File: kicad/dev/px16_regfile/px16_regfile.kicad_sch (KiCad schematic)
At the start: 336 parts, among them J1 Conn_02x12_Odd_Even, J2 Conn_02x12_Odd_Even, J3 Conn_02x12_Odd_Even, J4 Screw_Terminal_01x02, J5 Conn_02x12_Odd_Even, J6 Conn_02x12_Odd_Even, U1 74LS273, U10 74LS273, U11 74LS244, U12 74LS244, U13 74LS273, U14 74LS244, U15 74LS244, U16 74LS273, U17 74LS244, U18 74LS244, U19 74LS273, U2 74LS244, U20 74LS244, U21 74LS244, U22 74LS273, U23 74LS244, U24 74LS244, U25 74LS273, U26 74LS244, U27 74LS244, U28 74LS273, U29 74LS244, U3 74LS244, U30 74LS244, U31 74LS139, U32 74LS04, U33 74LS139, U34 74LS139, U35 74LS02, U36 74LS02, U37 74LS273, U38 74LS244, U39 74LS244, U4 74LS273, U40 74LS244, U41 74LS244, U42 74LS244, U43 74LS244, U44 74LS161, U45 74LS161, U46 74LS244, U47 74LS244, U48 74LS161, U49 74LS161, U5 74LS244, U50 74LS244, U51 74LS244, U52 74LS00, U53 74LS273, U54 74LS273, U55 74LS273, U56 74LS273, U57 74LS244, U58 74LS244, U59 74LS244, U6 74LS244, U60 74LS244, U7 74LS273, U8 74LS244, U9 74LS244

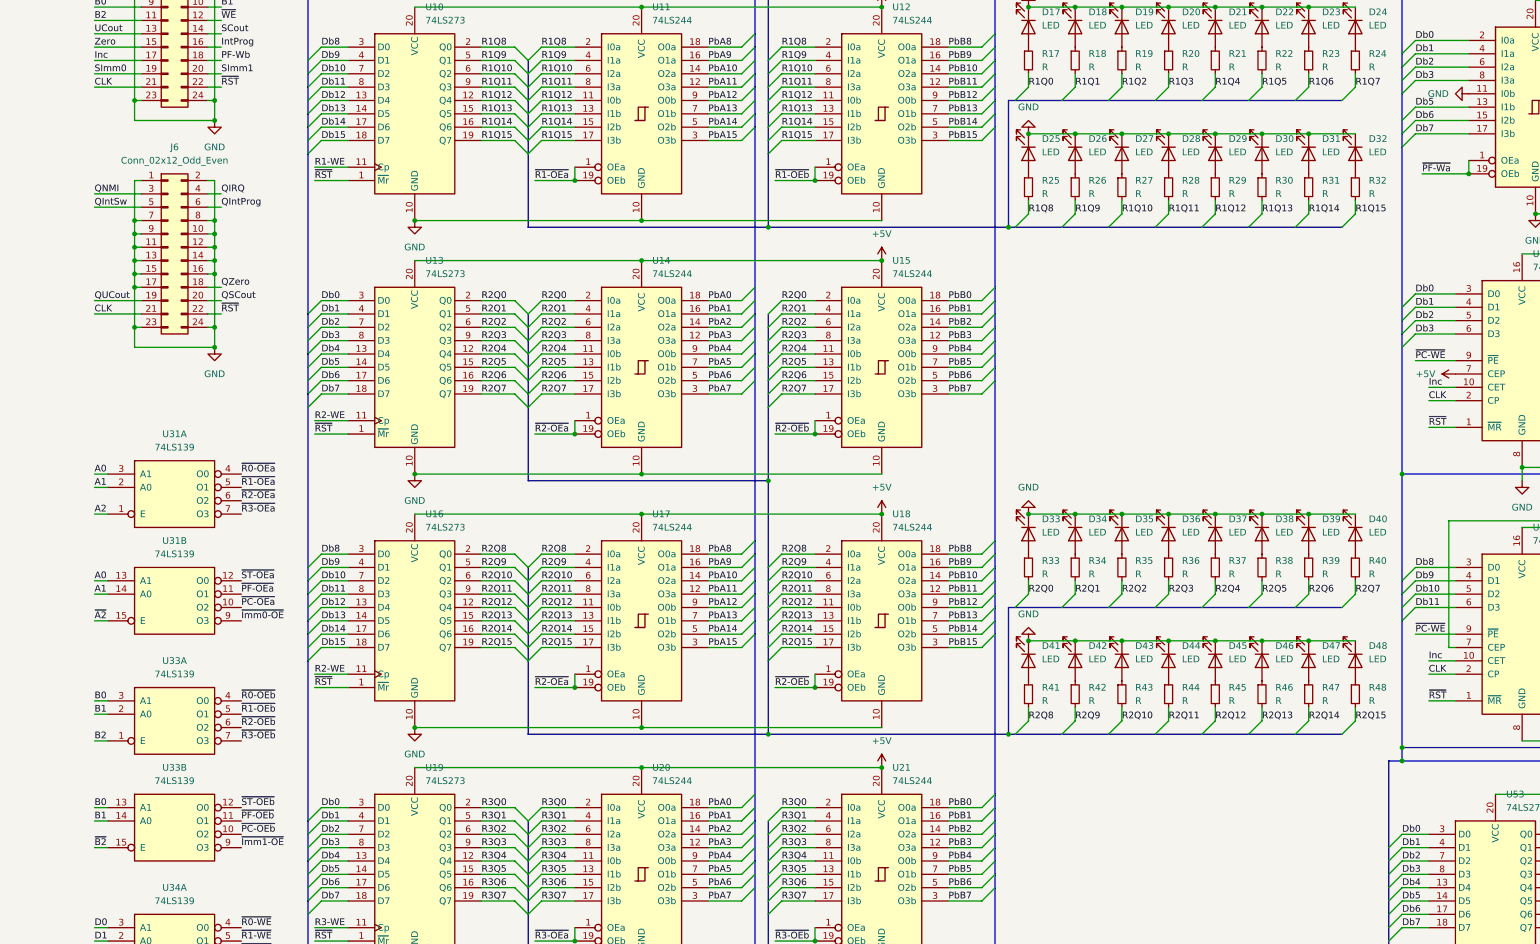
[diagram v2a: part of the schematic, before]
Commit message: Nearly completed the regfile.
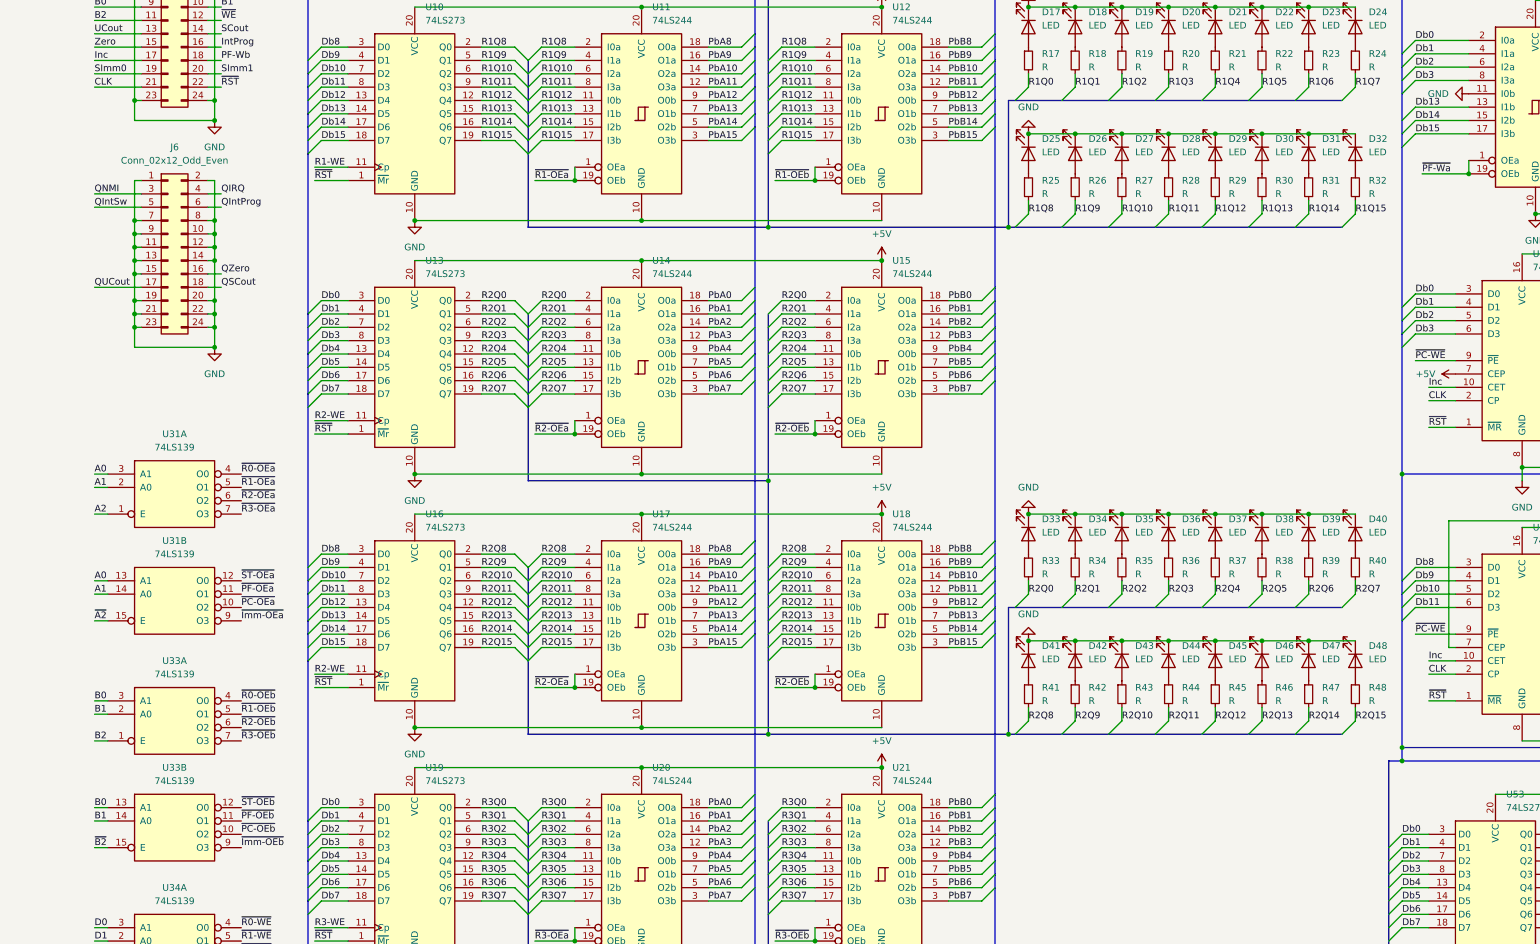
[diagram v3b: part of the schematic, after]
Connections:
- net ~{Imm0-OE} is gone; now on net ~{Imm-OEa}: U31.9 (O3)
- net ~{Imm1-OE} is gone; now on net ~{Imm-OEb}: U33.9 (O3)
- net CLK: no longer J6.21 (Pin_21)
- net Db13: now also U40.13 (I1b)
- net Db14: now also U40.15 (I2b)
- net Db15: now also U40.17 (I3b)
- net Db5: no longer U40.13 (I1b)
- net Db6: no longer U40.15 (I2b)
- net Db7: no longer U40.17 (I3b)
- net GND: now also J6.19 (Pin_19), J6.20 (Pin_20), J6.21 (Pin_21), J6.22 (Pin_22); no longer J6.16 (Pin_16), J6.17 (Pin_17)
- net QSCout: now also J6.18 (Pin_18); no longer J6.20 (Pin_20)
- net QUCout: now also J6.17 (Pin_17); no longer J6.19 (Pin_19)
- net QZero: now also J6.16 (Pin_16); no longer J6.18 (Pin_18)
- net ~{RST}: no longer J6.22 (Pin_22)
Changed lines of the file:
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@@
   (junction (at 172.72 528.32) (diameter 0) (color 0 0 0 0)
   )
+  (junction (at 134.62 256.54) (diameter 0) (color 0 0 0 0)
+  )
   (junction (at 581.66 401.32) (diameter 0) (color 0 0 0 0)
   )
@@
   (junction (at 394.97 337.82) (diameter 0) (color 0 0 0 0)
   )
-  (junction (at 134.62 248.92) (diameter 0) (color 0 0 0 0)
-  )
   (junction (at 119.38 127) (diameter 0) (color 0 0 0 0)
   )
@@
   (junction (at 431.8 185.42) (diameter 0) (color 0 0 0 0)
   )
+  (junction (at 134.62 254) (diameter 0) (color 0 0 0 0)
+  )
   (junction (at 590.55 298.45) (diameter 0) (color 0 0 0 0)
   )
@@
   (junction (at 334.01 511.81) (diameter 0) (color 0 0 0 0)
   )
+  (junction (at 119.38 256.54) (diameter 0) (color 0 0 0 0)
+  )
   (junction (at 581.66 298.45) (diameter 0) (color 0 0 0 0)
   )
@@
   (junction (at 119.38 172.72) (diameter 0) (color 0 0 0 0)
   )
+  (junction (at 119.38 254) (diameter 0) (color 0 0 0 0)
+  )
   (junction (at 554.99 401.32) (diameter 0) (color 0 0 0 0)
   )
@@
   (junction (at 383.54 285.75) (diameter 0) (color 0 0 0 0)
   )
-  (junction (at 119.38 251.46) (diameter 0) (color 0 0 0 0)
-  )
   (junction (at 285.75 240.03) (diameter 0) (color 0 0 0 0)
   )
@@
     (stroke (width 0) (type default) (color 0 0 0 0))
   )
+  (wire (pts (xy 119.38 254) (xy 120.65 254))
+    (stroke (width 0) (type default) (color 0 0 0 0))
+  )
   (bus (pts (xy 194.31 220.98) (xy 194.31 223.52))
     (stroke (width 0) (type default) (color 0 0 0 0))
@@
     (stroke (width 0) (type default) (color 0 0 0 0))
   )
-  (wire (pts (xy 111.76 254) (xy 120.65 254))
+  (wire (pts (xy 111.76 251.46) (xy 120.65 251.46))
     (stroke (width 0) (type default) (color 0 0 0 0))
   )
@@
     (stroke (width 0) (type default) (color 0 0 0 0))
   )
-  (wire (pts (xy 133.35 254) (xy 135.89 254))
+  (wire (pts (xy 133.35 251.46) (xy 135.89 251.46))
     (stroke (width 0) (type default) (color 0 0 0 0))
   )
@@
     (stroke (width 0) (type default) (color 0 0 0 0))
   )
-  (wire (pts (xy 133.35 251.46) (xy 135.89 251.46))
+  (wire (pts (xy 133.35 248.92) (xy 135.89 248.92))
     (stroke (width 0) (type default) (color 0 0 0 0))
   )
@@
     (stroke (width 0) (type default) (color 0 0 0 0))
   )
+  (wire (pts (xy 119.38 256.54) (xy 120.65 256.54))
+    (stroke (width 0) (type default) (color 0 0 0 0))
+  )
   (wire (pts (xy 119.38 238.76) (xy 120.65 238.76))
     (stroke (width 0) (type default) (color 0 0 0 0))
@@
     (stroke (width 0) (type default) (color 0 0 0 0))
   )
-  (wire (pts (xy 134.62 246.38) (xy 134.62 248.92))
+  (wire (pts (xy 134.62 246.38) (xy 134.62 254))
     (stroke (width 0) (type default) (color 0 0 0 0))
   )
@@
     (stroke (width 0) (type default) (color 0 0 0 0))
   )
-  (wire (pts (xy 119.38 248.92) (xy 119.38 251.46))
+  (wire (pts (xy 119.38 248.92) (xy 119.38 254))
     (stroke (width 0) (type default) (color 0 0 0 0))
   )
@@
     (stroke (width 0) (type default) (color 0 0 0 0))
   )
-  (wire (pts (xy 134.62 248.92) (xy 134.62 259.08))
-    (stroke (width 0) (type default) (color 0 0 0 0))
-  )
   (bus (pts (xy 605.79 316.23) (xy 596.9 316.23))
     (stroke (width 0) (type default) (color 0 0 0 0))
@@
     (stroke (width 0) (type default) (color 0 0 0 0))
   )
-  (wire (pts (xy 119.38 251.46) (xy 120.65 251.46))
-    (stroke (width 0) (type default) (color 0 0 0 0))
-  )
   (wire (pts (xy 289.56 511.81) (xy 298.45 511.81))
     (stroke (width 0) (type default) (color 0 0 0 0))
@@
     (stroke (width 0) (type default) (color 0 0 0 0))
   )
+  (wire (pts (xy 133.35 256.54) (xy 134.62 256.54))
+    (stroke (width 0) (type default) (color 0 0 0 0))
+  )
   (wire (pts (xy 241.3 182.88) (xy 248.92 182.88))
     (stroke (width 0) (type default) (color 0 0 0 0))
@@
     (stroke (width 0) (type default) (color 0 0 0 0))
   )
+  (wire (pts (xy 134.62 256.54) (xy 134.62 259.08))
+    (stroke (width 0) (type default) (color 0 0 0 0))
+  )
   (bus (pts (xy 539.75 320.04) (xy 539.75 353.06))
     (stroke (width 0) (type default) (color 0 0 0 0))
@@
     (stroke (width 0) (type default) (color 0 0 0 0))
   )
-  (wire (pts (xy 111.76 256.54) (xy 120.65 256.54))
-    (stroke (width 0) (type default) (color 0 0 0 0))
-  )
   (wire (pts (xy 334.01 294.64) (xy 342.9 294.64))
     (stroke (width 0) (type default) (color 0 0 0 0))
@@
     (stroke (width 0) (type default) (color 0 0 0 0))
   )
-  (wire (pts (xy 119.38 251.46) (xy 119.38 259.08))
-    (stroke (width 0) (type default) (color 0 0 0 0))
-  )
   (bus (pts (xy 360.68 214.63) (xy 360.68 219.71))
     (stroke (width 0) (type default) (color 0 0 0 0))
@@
     (stroke (width 0) (type default) (color 0 0 0 0))
   )
+  (wire (pts (xy 134.62 254) (xy 134.62 256.54))
+    (stroke (width 0) (type default) (color 0 0 0 0))
+  )
   (wire (pts (xy 452.12 425.45) (xy 459.74 425.45))
     (stroke (width 0) (type default) (color 0 0 0 0))
@@
     (stroke (width 0) (type default) (color 0 0 0 0))
   )
-  (wire (pts (xy 133.35 256.54) (xy 135.89 256.54))
-    (stroke (width 0) (type default) (color 0 0 0 0))
-  )
   (wire (pts (xy 485.14 270.51) (xy 491.49 270.51))
     (stroke (width 0) (type default) (color 0 0 0 0))
@@
     (stroke (width 0) (type default) (color 0 0 0 0))
   )
+  (wire (pts (xy 119.38 256.54) (xy 119.38 259.08))
+    (stroke (width 0) (type default) (color 0 0 0 0))
+  )
   (bus (pts (xy 240.03 500.38) (xy 240.03 502.92))
     (stroke (width 0) (type default) (color 0 0 0 0))
@@
     (stroke (width 0) (type default) (color 0 0 0 0))
   )
+  (wire (pts (xy 133.35 254) (xy 134.62 254))
+    (stroke (width 0) (type default) (color 0 0 0 0))
+  )
   (wire (pts (xy 274.32 254) (xy 280.67 254))
     (stroke (width 0) (type default) (color 0 0 0 0))
@@
     (stroke (width 0) (type default) (color 0 0 0 0))
   )
-  (wire (pts (xy 133.35 248.92) (xy 134.62 248.92))
-    (stroke (width 0) (type default) (color 0 0 0 0))
-  )
   (wire (pts (xy 530.86 152.4) (xy 537.21 152.4))
     (stroke (width 0) (type default) (color 0 0 0 0))
@@
     (stroke (width 0) (type default) (color 0 0 0 0))
   )
+  (wire (pts (xy 119.38 254) (xy 119.38 256.54))
+    (stroke (width 0) (type default) (color 0 0 0 0))
+  )
   (bus (pts (xy 283.21 170.18) (xy 283.21 172.72))
     (stroke (width 0) (type default) (color 0 0 0 0))
@@
     (effects (font (size 1.27 1.27)) (justify left bottom))
   )
-  (label "~{Imm0-OE}" (at 139.7 314.96 0)
+  (label "~{Imm-OEa}" (at 139.7 314.96 0)
     (effects (font (size 1.27 1.27)) (justify left bottom))
   )
@@
     (effects (font (size 1.27 1.27)) (justify left bottom))
   )
-  (label "QZero" (at 135.89 251.46 0)
+  (label "QZero" (at 135.89 248.92 0)
     (effects (font (size 1.27 1.27)) (justify left bottom))
   )
@@
     (effects (font (size 1.27 1.27)) (justify left bottom))
   )
-  (label "CLK" (at 111.76 256.54 0)
-    (effects (font (size 1.27 1.27)) (justify left bottom))
-  )
   (label "STQ4" (at 185.42 457.2 0)
     (effects (font (size 1.27 1.27)) (justify left bottom))
@@
     (effects (font (size 1.27 1.27)) (justify left bottom))
   )
-  (label "Db6" (at 363.22 219.71 0)
+  (label "Db14" (at 363.22 219.71 0)
     (effects (font (size 1.27 1.27)) (justify left bottom))
   )
@@
     (effects (font (size 1.27 1.27)) (justify left bottom))
   )
-  (label "~{Imm1-OE}" (at 139.7 358.14 0)
+  (label "~{Imm-OEb}" (at 139.7 358.14 0)
     (effects (font (size 1.27 1.27)) (justify left bottom))
   )
@@
     (effects (font (size 1.27 1.27)) (justify left bottom))
   )
-  (label "Db7" (at 363.22 222.25 0)
+  (label "Db15" (at 363.22 222.25 0)
     (effects (font (size 1.27 1.27)) (justify left bottom))
   )
@@
     (effects (font (size 1.27 1.27)) (justify left bottom))
   )
-  (label "QSCout" (at 135.89 254 0)
+  (label "QSCout" (at 135.89 251.46 0)
     (effects (font (size 1.27 1.27)) (justify left bottom))
   )
@@
     (effects (font (size 1.27 1.27)) (justify left bottom))
   )
-  (label "QUCout" (at 111.76 254 0)
+  (label "QUCout" (at 111.76 251.46 0)
     (effects (font (size 1.27 1.27)) (justify left bottom))
   )
@@
     (effects (font (size 1.27 1.27)) (justify left bottom))
   )
-  (label "Db5" (at 363.22 217.17 0)
+  (label "Db13" (at 363.22 217.17 0)
     (effects (font (size 1.27 1.27)) (justify left bottom))
   )
@@
     (effects (font (size 1.27 1.27)) (justify left bottom))
   )
-  (label "~{RST}" (at 135.89 256.54 0)
-    (effects (font (size 1.27 1.27)) (justify left bottom))
-  )

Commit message: Oops! DRC says your design is broken!
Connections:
- net CLK: now also U52.4; no longer U32.9
- net Imm-WEa: now also U32.8; no longer U52.6
- net at U35.12, U35.3, U35.6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: now also U52.6; no longer U32.8
- net ~{WE} renamed WE
- net WE: now also U52.5
- new net: U32.9, U52.3
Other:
- moved on the sheet: U32D, U52B
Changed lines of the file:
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@@
   (junction (at 134.62 170.18) (diameter 0) (color 0 0 0 0)
   )
-  (junction (at 59.69 257.81) (diameter 0) (color 0 0 0 0)
-  )
   (junction (at 459.74 330.2) (diameter 0) (color 0 0 0 0)
   )
@@
     (stroke (width 0) (type default) (color 0 0 0 0))
   )
-  (wire (pts (xy 59.69 255.27) (xy 59.69 257.81))
-    (stroke (width 0) (type default) (color 0 0 0 0))
-  )
   (wire (pts (xy 316.23 307.34) (xy 316.23 309.88))
     (stroke (width 0) (type default) (color 0 0 0 0))
@@
     (stroke (width 0) (type default) (color 0 0 0 0))
   )
-  (wire (pts (xy 34.29 210.82) (xy 38.1 210.82))
+  (wire (pts (xy 34.29 208.28) (xy 38.1 208.28))
     (stroke (width 0) (type default) (color 0 0 0 0))
   )
@@
     (stroke (width 0) (type default) (color 0 0 0 0))
   )
-  (wire (pts (xy 59.69 257.81) (xy 59.69 260.35))
-    (stroke (width 0) (type default) (color 0 0 0 0))
-  )
   (bus (pts (xy 340.36 312.42) (xy 331.47 312.42))
     (stroke (width 0) (type default) (color 0 0 0 0))
@@
     (stroke (width 0) (type default) (color 0 0 0 0))
   )
+  (wire (pts (xy 34.29 213.36) (xy 38.1 213.36))
+    (stroke (width 0) (type default) (color 0 0 0 0))
+  )
   (wire (pts (xy 228.6 454.66) (xy 234.95 454.66))
     (stroke (width 0) (type default) (color 0 0 0 0))
@@
     (effects (font (size 1.27 1.27)) (justify left bottom))
   )
-  (label "CLK" (at 34.29 210.82 0)
+  (label "CLK" (at 34.29 208.28 0)
     (effects (font (size 1.27 1.27)) (justify left bottom))
   )
@@
     (effects (font (size 1.27 1.27)) (justify left bottom))
   )
-  (label "~{WE}" (at 135.89 200.66 0)
+  (label "WE" (at 135.89 200.66 0)
     (effects (font (size 1.27 1.27)) (justify left bottom))
   )
@@
     (effects (font (size 1.27 1.27)) (justify left bottom))
   )
+  (label "WE" (at 34.29 213.36 0)
+    (effects (font (size 1.27 1.27)) (justify left bottom))
+  )
   (label "PCQ8" (at 499.11 304.8 0)
     (effects (font (size 1.27 1.27)) (justify left bottom))
@@
     (pin "2")
   )
-  (symbol (lib_id "74xx:74LS00") (at 67.31 257.81 0) (unit 2)
+  (symbol (lib_id "74xx:74LS00") (at 45.72 210.82 0) (unit 2)
     (in_bom yes) (on_board yes) (fields_autoplaced)
-    (property "Reference" "U52" (id 0) (at 67.31 248.92 0))
-    (property "Value" "74LS00" (id 1) (at 67.31 251.46 0))
-    (property "Footprint" "Package_DIP:DIP-14_W7.62mm" (id 2) (at 67.31 257.81 0)
+    (property "Reference" "U52" (id 0) (at 45.72 201.93 0))
+    (property "Value" "74LS00" (id 1) (at 45.72 204.47 0))
+    (property "Footprint" "Package_DIP:DIP-14_W7.62mm" (id 2) (at 45.72 210.82 0)
       (effects (font (size 1.27 1.27)) hide)
     )
-    (property "Datasheet" "http://www.ti.com/lit/gpn/sn74ls00" (id 3) (at 67.31 257.81 0)
+    (property "Datasheet" "http://www.ti.com/lit/gpn/sn74ls00" (id 3) (at 45.72 210.82 0)
       (effects (font (size 1.27 1.27)) hide)
     )
@@
     (pin "2")
   )
-  (symbol (lib_id "74xx:74LS04") (at 45.72 210.82 0) (unit 4)
+  (symbol (lib_id "74xx:74LS04") (at 67.31 257.81 0) (unit 4)
     (in_bom yes) (on_board yes) (fields_autoplaced)
-    (property "Reference" "U32" (id 0) (at 45.72 201.93 0))
-    (property "Value" "74LS04" (id 1) (at 45.72 204.47 0))
-    (property "Footprint" "Package_DIP:DIP-14_W7.62mm" (id 2) (at 45.72 210.82 0)
+    (property "Reference" "U32" (id 0) (at 67.31 248.92 0))
+    (property "Value" "74LS04" (id 1) (at 67.31 251.46 0))
+    (property "Footprint" "Package_DIP:DIP-14_W7.62mm" (id 2) (at 67.31 257.81 0)
       (effects (font (size 1.27 1.27)) hide)
     )
-    (property "Datasheet" "http://www.ti.com/lit/gpn/sn74LS04" (id 3) (at 45.72 210.82 0)
+    (property "Datasheet" "http://www.ti.com/lit/gpn/sn74LS04" (id 3) (at 67.31 257.81 0)
       (effects (font (size 1.27 1.27)) hide)
     )

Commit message: Small tweaks.
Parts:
- added H1: MountingHole_Pad, symbol Mechanical:MountingHole_Pad
- added H2, H3, H4, H5, H6, H7, H8: MountingHole_Pad, MountingHole:MountingHole_3mm_Pad, symbol Mechanical:MountingHole_Pad
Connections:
- net GND: now also H1.1, H2.1, H3.1, H4.1, H5.1, H6.1, H7.1, H8.1
